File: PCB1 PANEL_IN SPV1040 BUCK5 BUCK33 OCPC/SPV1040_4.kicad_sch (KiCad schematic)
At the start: 14 parts, among them J2 SOLAR, U2 SPV1040TTR

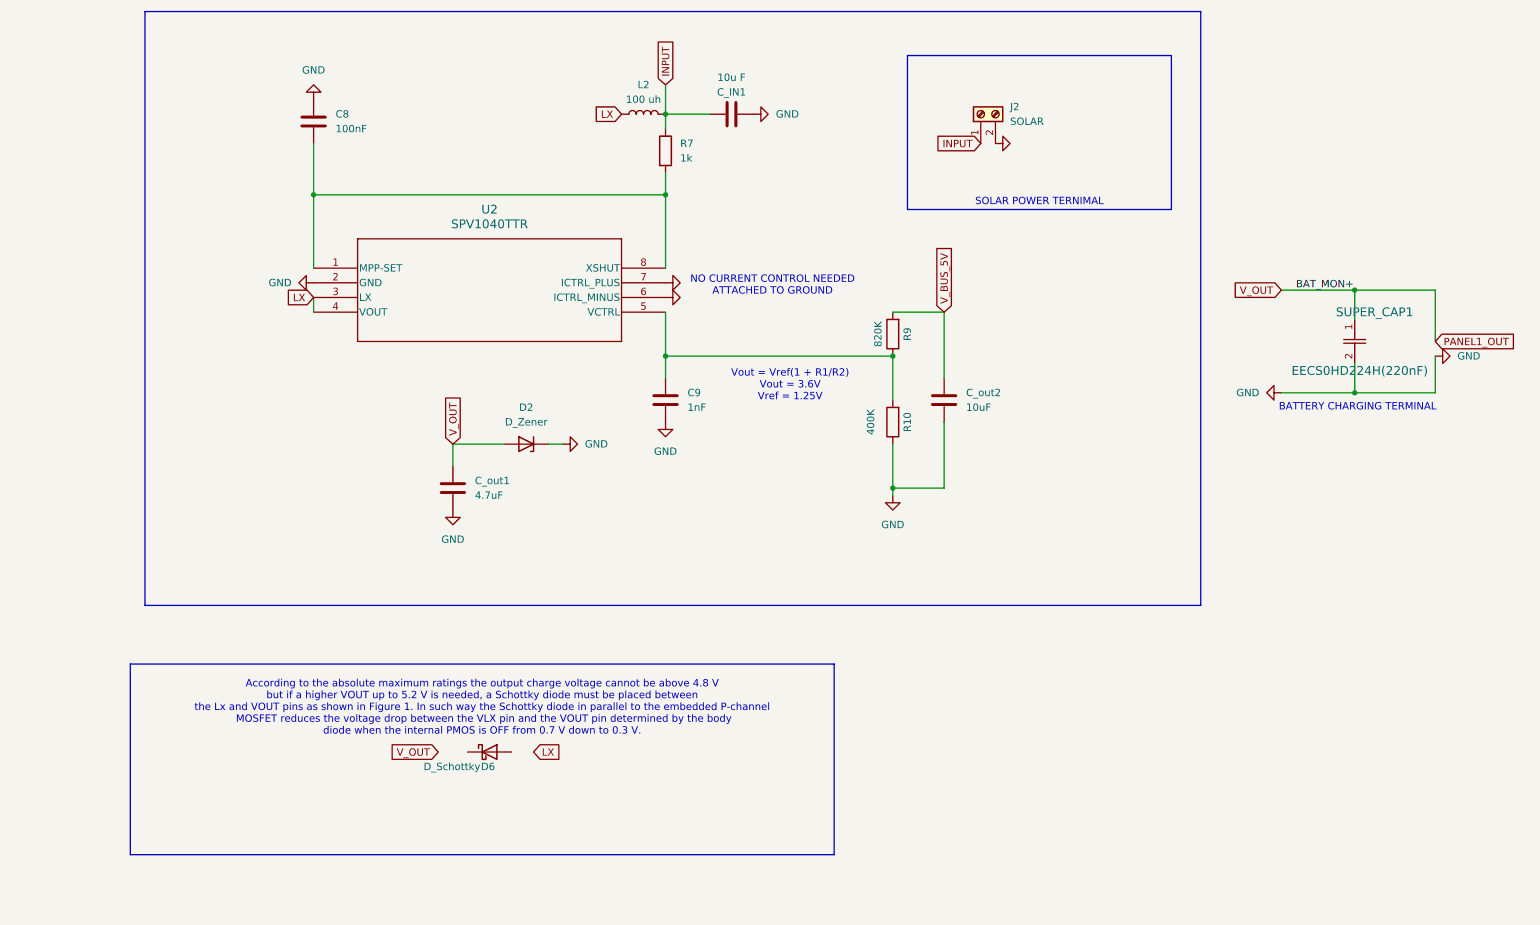
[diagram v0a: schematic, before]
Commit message: Changes
Added bucks from old work
and copied SPV
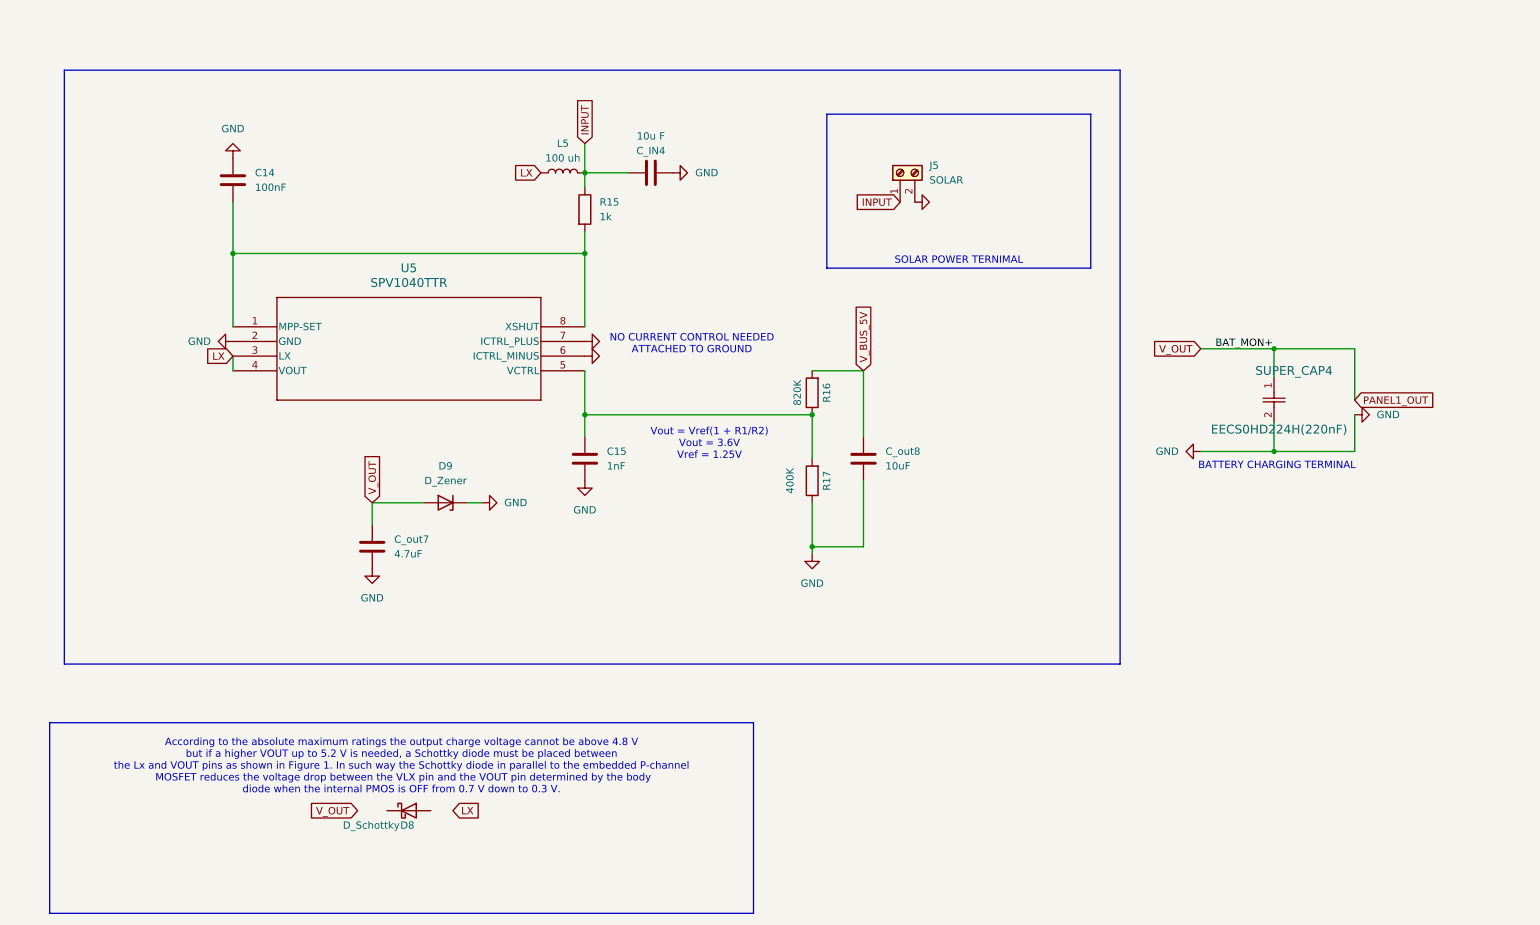
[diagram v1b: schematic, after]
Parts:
- removed C8: 100nF, Capacitor_SMD:C_0603_1608Metric, symbol Device:C
- removed C9: 1nF, Capacitor_SMD:C_0603_1608Metric, symbol Device:C
- removed C_IN1: 10u F, Capacitor_SMD:C_0603_1608Metric, symbol Device:C
- removed C_out1: 4.7uF, Capacitor_SMD:C_0603_1608Metric, symbol Device:C
- removed C_out2: 10uF, Capacitor_SMD:C_0603_1608Metric, symbol Device:C
- removed D2: D_Zener, Diode_SMD:D_1210_3225Metric, symbol Device:D_Zener
- removed D6: D_Schottky, symbol Device:D_Schottky
- removed J2: SOLAR, TerminalBlock_Phoenix:TerminalBlock_Phoenix_PT-1,5-2-5.0-H_1x02_P5.00mm_Horizontal, symbol Connector:Screw_Terminal_01x02
- removed L2: 100 uh, Inductor_SMD:L_Coilcraft_XAL6060-XXX, symbol Device:L
- removed R10: 400K, Resistor_SMD:R_0603_1608Metric, symbol Device:R
- removed R7: 1k, Resistor_SMD:R_0603_1608Metric, symbol Device:R
- removed R9: 820K, Resistor_SMD:R_0603_1608Metric, symbol Device:R
- removed SUPER_CAP1: EECS0HD224H(220nF), SPV1040T:CAP_EECS0_H_PAN, symbol 2024-06-08_06-57-05:super_capacitor
- removed U2: SPV1040TTR, SPV1040:SOP65P640X120-8N, symbol 2024-06-07_14-27-39:SPV1040TTR
- added C14: 100nF, Capacitor_SMD:C_0603_1608Metric, symbol Device:C
- added C15: 1nF, Capacitor_SMD:C_0603_1608Metric, symbol Device:C
- added C_IN4: 10u F, Capacitor_SMD:C_0603_1608Metric, symbol Device:C
- added C_out7: 4.7uF, Capacitor_SMD:C_0603_1608Metric, symbol Device:C
- added C_out8: 10uF, Capacitor_SMD:C_0603_1608Metric, symbol Device:C
- added D8: D_Schottky, symbol Device:D_Schottky
- added D9: D_Zener, Diode_SMD:D_1210_3225Metric, symbol Device:D_Zener
- added J5: SOLAR, TerminalBlock_Phoenix:TerminalBlock_Phoenix_PT-1,5-2-5.0-H_1x02_P5.00mm_Horizontal, symbol Connector:Screw_Terminal_01x02
- added L5: 100 uh, Inductor_SMD:L_Coilcraft_XAL6060-XXX, symbol Device:L
- added R15: 1k, Resistor_SMD:R_0603_1608Metric, symbol Device:R
- added R16: 820K, Resistor_SMD:R_0603_1608Metric, symbol Device:R
- added R17: 400K, Resistor_SMD:R_0603_1608Metric, symbol Device:R
- added SUPER_CAP4: EECS0HD224H(220nF), SPV1040T:CAP_EECS0_H_PAN, symbol 2024-06-08_06-57-05:super_capacitor
- added U5: SPV1040TTR, SPV1040:SOP65P640X120-8N, symbol 2024-06-07_14-27-39:SPV1040TTR
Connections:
- net GND: now also C14.1, C15.2, C_IN4.2, C_out7.1, C_out8.2, D9.1 (K), J5.2 (Pin_2), R17.1, SUPER_CAP4.2, U5.2 (GND), U5.6 (ICTRL_MINUS), U5.7 (ICTRL_PLUS)
- net INPUT: now also C_IN4.1, J5.1 (Pin_1), L5.2, R15.1
- net LX: now also L5.1, U5.3 (LX), U5.4 (VOUT)
- net PANEL1_OUT: now also C_out7.2, D9.2 (A), SUPER_CAP4.1
- net V_BUS_5V: now also C_out8.1, R16.2
- new net: C14.2, R15.2, U5.1 (MPP-SET), U5.8 (XSHUT)
- new net: C15.1, R16.1, R17.2, U5.5 (VCTRL)
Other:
- company: TEAM ANANT -> (none)
- title: SOLAR CHARGER -> (none)
